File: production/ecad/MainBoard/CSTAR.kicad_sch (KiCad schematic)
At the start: 0 parts

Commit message: Button + RGB IO schematic
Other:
- added sheet CSTAR-IO (cstar-io.kicad_sch)
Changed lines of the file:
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@@
+    )
+  )
+  (sheet (at 191.77 99.06) (size 18.415 15.24) (fields_autoplaced)
+    (stroke (width 0.1524) (type solid))
+    (fill (color 0 0 0 0.0000))
+    (property "Sheetname" "CSTAR-IO" (at 191.77 98.3484 0)
+      (effects (font (size 1.27 1.27)) (justify left bottom))
+    )
+    (property "Sheetfile" "cstar-io.kicad_sch" (at 191.77 114.8846 0)
+      (effects (font (size 1.27 1.27)) (justify left top))
+    )
+    (instances
+      (project "CSTAR"
+        (path "/cd9fa943-c6eb-468b-990c-ea873c442553" (page "7"))
+      )
     )
   )

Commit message: Update of gitignore and main sch
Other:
- sheet CSTAR-Drive ports: added Ch.A Motor 1, Ch.A Motor 2, Ch.B Motor 1, Ch.B Motor 2, DECAY MOTOR 1, DECAY MOTOR 2, GND Motor 1, GND Motor 2, I0 MOTOR 1, I0 MOTOR 2, I1 MOTOR 1, I1 MOTOR 2, I2 MOTOR 1, I2 MOTOR 2, I3 MOTOR 1, I3 MOTOR 2, I4 MOTOR 1, I4 MOTOR 2, IN1 MOTOR 1, IN1 MOTOR 2, IN2 MOTOR 1, IN2 MOTOR 2, OUT1 MOTOR 1, OUT1 MOTOR 2, OUT2 MOTOR 1, OUT2 MOTOR 2, VCC Motor 1, VCC Motor 2, nFAULT MOTOR 1, nFAULT MOTOR 2, nRESET MOTOR 1, nRESET MOTOR 2, nSLEEP MOTOR 1, nSLEEP MOTOR 2; removed none
- sheet CSTAR-IO ports: added BATT_IN, RBG_Green_Control, RGB_Blue_Control, RGB_Red_Control; removed none
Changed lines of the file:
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@@
     )
   )
-  (sheet (at 191.77 99.06) (size 18.415 15.24) (fields_autoplaced)
+  (sheet (at 191.77 99.06) (size 34.925 27.305) (fields_autoplaced)
     (stroke (width 0.1524) (type solid))
     (fill (color 0 0 0 0.0000))
@@
       (effects (font (size 1.27 1.27)) (justify left bottom))
     )
-    (property "Sheetfile" "cstar-io.kicad_sch" (at 191.77 114.8846 0)
+    (property "Sheetfile" "cstar-io.kicad_sch" (at 191.77 126.9496 0)
       (effects (font (size 1.27 1.27)) (justify left top))
+    )
+    (pin "RGB_Red_Control" input (at 191.77 104.14 180)
+      (effects (font (size 1.27 1.27)) (justify left))
+    )
+    (pin "RBG_Green_Control" input (at 191.77 110.49 180)
+      (effects (font (size 1.27 1.27)) (justify left))
+    )
+    (pin "RGB_Blue_Control" input (at 191.77 116.84 180)
+      (effects (font (size 1.27 1.27)) (justify left))
+    )
+    (pin "BATT_IN" input (at 226.695 104.14 0)
+      (effects (font (size 1.27 1.27)) (justify right))
     )
     (instances
@@
     )
   )
-  (sheet (at 179.705 29.845) (size 45.085 45.085) (fields_autoplaced)
+  (sheet (at 172.72 20.32) (size 71.12 61.595) (fields_autoplaced)
     (stroke (width 0.1524) (type solid))
     (fill (color 0 0 0 0.0000))
-    (property "Sheetname" "CSTAR-Drive" (at 179.705 29.1334 0)
+    (property "Sheetname" "CSTAR-Drive" (at 172.72 19.6084 0)
       (effects (font (size 1.27 1.27)) (justify left bottom))
     )
-    (property "Sheetfile" "cstar-drive.kicad_sch" (at 179.705 75.5146 0)
+    (property "Sheetfile" "cstar-drive.kicad_sch" (at 172.72 82.4996 0)
       (effects (font (size 1.27 1.27)) (justify left top))
     )
+    (pin "Ch.B Motor 1" input (at 172.72 22.86 180)
+      (effects (font (size 1.27 1.27)) (justify left))
+    )
+    (pin "OUT1 MOTOR 1" passive (at 243.84 37.465 0)
+      (effects (font (size 1.27 1.27)) (justify right))
+    )
+    (pin "OUT2 MOTOR 1" passive (at 243.84 43.815 0)
+      (effects (font (size 1.27 1.27)) (justify right))
+    )
+    (pin "VCC Motor 1" input (at 243.84 24.765 0)
+      (effects (font (size 1.27 1.27)) (justify right))
+    )
+    (pin "Ch.A Motor 1" input (at 172.72 26.035 180)
+      (effects (font (size 1.27 1.27)) (justify left))
+    )
+    (pin "GND Motor 1" input (at 243.84 76.2 0)
+      (effects (font (size 1.27 1.27)) (justify right))
+    )
+    (pin "OUT2 MOTOR 2" passive (at 243.84 50.8 0)
+      (effects (font (size 1.27 1.27)) (justify right))
+    )
+    (pin "OUT1 MOTOR 2" passive (at 243.84 56.515 0)
+      (effects (font (size 1.27 1.27)) (justify right))
+    )
+    (pin "IN1 MOTOR 2" input (at 172.72 31.75 180)
+      (effects (font (size 1.27 1.27)) (justify left))
+    )
+    (pin "nFAULT MOTOR 1" output (at 172.72 34.29 180)
+      (effects (font (size 1.27 1.27)) (justify left))
+    )
+    (pin "nFAULT MOTOR 2" output (at 172.72 44.45 180)
+      (effects (font (size 1.27 1.27)) (justify left))
+    )
+    (pin "DECAY MOTOR 2" input (at 172.72 52.07 180)
+      (effects (font (size 1.27 1.27)) (justify left))
+    )
+    (pin "I0 MOTOR 2" input (at 172.72 46.99 180)
+      (effects (font (size 1.27 1.27)) (justify left))
+    )
+    (pin "nSLEEP MOTOR 2" input (at 172.72 49.53 180)
+      (effects (font (size 1.27 1.27)) (justify left))
+    )
+    (pin "I2 MOTOR 2" input (at 172.72 41.91 180)
+      (effects (font (size 1.27 1.27)) (justify left))
+    )
+    (pin "nRESET MOTOR 2" input (at 172.72 54.61 180)
+      (effects (font (size 1.27 1.27)) (justify left))
+    )
+    (pin "I3 MOTOR 2" input (at 172.72 39.37 180)
+      (effects (font (size 1.27 1.27)) (justify left))
+    )
+    (pin "I4 MOTOR 2" input (at 172.72 60.325 180)
+      (effects (font (size 1.27 1.27)) (justify left))
+    )
+    (pin "I1 MOTOR 2" input (at 172.72 68.58 180)
+      (effects (font (size 1.27 1.27)) (justify left))
+    )
+    (pin "IN2 MOTOR 2" input (at 172.72 71.12 180)
+      (effects (font (size 1.27 1.27)) (justify left))
+    )
+    (pin "GND Motor 2" input (at 172.72 73.66 180)
+      (effects (font (size 1.27 1.27)) (justify left))
+    )
+    (pin "Ch.B Motor 2" input (at 172.72 76.2 180)
+      (effects (font (size 1.27 1.27)) (justify left))
+    )
+    (pin "Ch.A Motor 2" input (at 172.72 78.74 180)
+      (effects (font (size 1.27 1.27)) (justify left))
+    )
+    (pin "VCC Motor 2" input (at 243.84 27.94 0)
+      (effects (font (size 1.27 1.27)) (justify right))
+    )
+    (pin "DECAY MOTOR 1" input (at 198.12 81.915 270)
+      (effects (font (size 1.27 1.27)) (justify left))
+    )
+    (pin "I4 MOTOR 1" input (at 201.93 81.915 270)
+      (effects (font (size 1.27 1.27)) (justify left))
+    )
+    (pin "nRESET MOTOR 1" input (at 201.93 81.915 270)
+      (effects (font (size 1.27 1.27)) (justify left))
+    )
+    (pin "nSLEEP MOTOR 1" input (at 206.375 81.915 270)
+      (effects (font (size 1.27 1.27)) (justify left))
+    )
+    (pin "IN2 MOTOR 1" input (at 210.185 81.915 270)
+      (effects (font (size 1.27 1.27)) (justify left))
+    )
+    (pin "I0 MOTOR 1" input (at 214.63 81.915 270)
+      (effects (font (size 1.27 1.27)) (justify left))
+    )
+    (pin "IN1 MOTOR 1" input (at 215.265 81.915 270)
+      (effects (font (size 1.27 1.27)) (justify left))
+    )
+    (pin "I3 MOTOR 1" input (at 219.075 81.915 270)
+      (effects (font (size 1.27 1.27)) (justify left))
+    )
+    (pin "I2 MOTOR 1" input (at 223.52 81.915 270)
+      (effects (font (size 1.27 1.27)) (justify left))
+    )
+    (pin "I1 MOTOR 1" input (at 227.965 81.915 270)
+      (effects (font (size 1.27 1.27)) (justify left))
+    )
     (instances

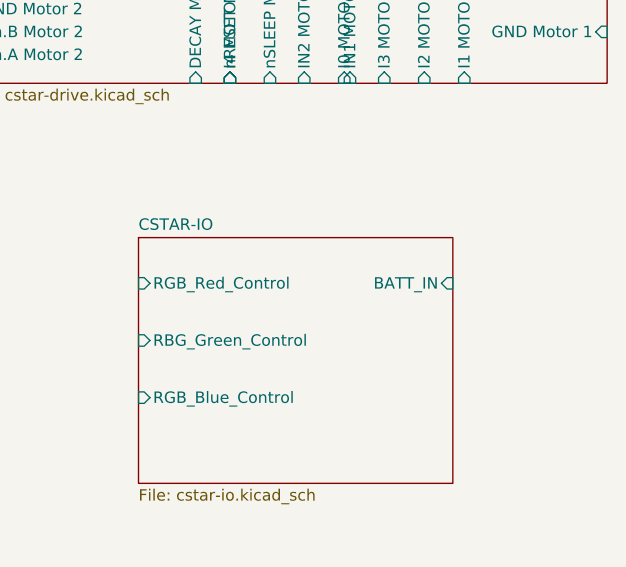
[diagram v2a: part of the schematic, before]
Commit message: updated battery connection net name
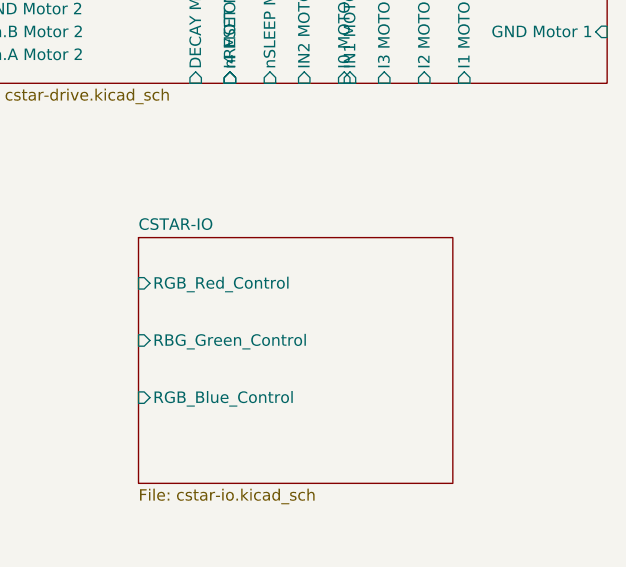
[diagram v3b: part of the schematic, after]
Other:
- sheet CSTAR-IO ports: added none; removed BATT_IN
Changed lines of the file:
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@@
       (effects (font (size 1.27 1.27)) (justify left))
-    )
-    (pin "BATT_IN" input (at 226.695 104.14 0)
-      (effects (font (size 1.27 1.27)) (justify right))
     )
     (instances

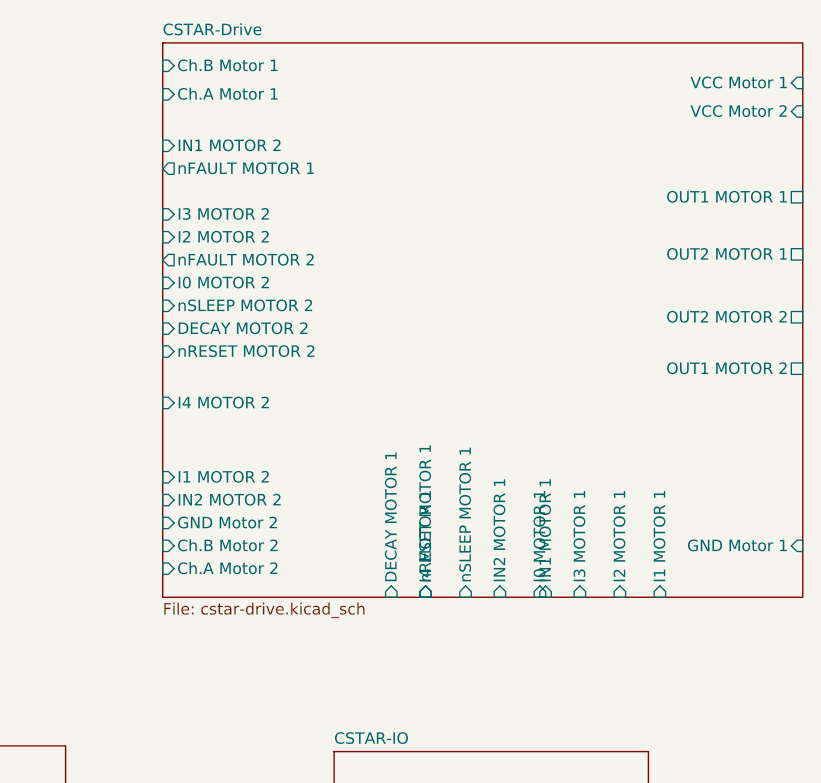
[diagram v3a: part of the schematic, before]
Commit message: updated hierarchical schematics
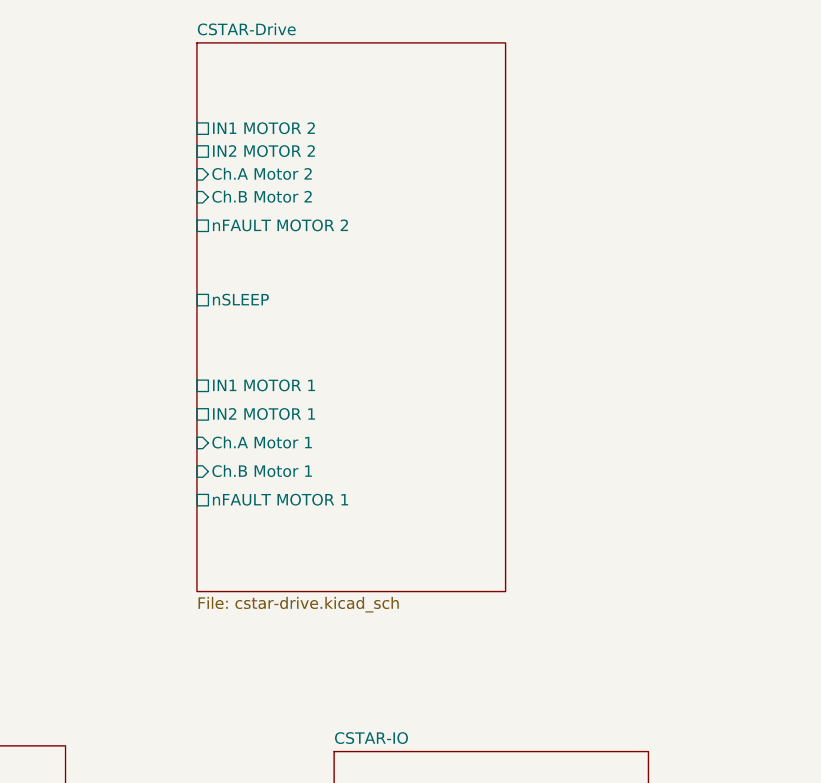
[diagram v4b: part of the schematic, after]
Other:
- sheet CSTAR-Drive ports: added nSLEEP; removed DECAY MOTOR 1, DECAY MOTOR 2, GND Motor 1, GND Motor 2, I0 MOTOR 1, I0 MOTOR 2, I1 MOTOR 1, I1 MOTOR 2, I2 MOTOR 1, I2 MOTOR 2, I3 MOTOR 1, I3 MOTOR 2, I4 MOTOR 1, I4 MOTOR 2, OUT1 MOTOR 1, OUT1 MOTOR 2, OUT2 MOTOR 1, OUT2 MOTOR 2, VCC Motor 1, VCC Motor 2, nRESET MOTOR 1, nRESET MOTOR 2, nSLEEP MOTOR 1, nSLEEP MOTOR 2
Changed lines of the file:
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@@
     )
   )
-  (sheet (at 172.72 20.32) (size 71.12 61.595) (fields_autoplaced)
+  (sheet (at 176.53 20.32) (size 34.29 60.96) (fields_autoplaced)
     (stroke (width 0.1524) (type solid))
     (fill (color 0 0 0 0.0000))
-    (property "Sheetname" "CSTAR-Drive" (at 172.72 19.6084 0)
+    (property "Sheetname" "CSTAR-Drive" (at 176.53 19.6084 0)
       (effects (font (size 1.27 1.27)) (justify left bottom))
     )
-    (property "Sheetfile" "cstar-drive.kicad_sch" (at 172.72 82.4996 0)
+    (property "Sheetfile" "cstar-drive.kicad_sch" (at 176.53 81.8646 0)
       (effects (font (size 1.27 1.27)) (justify left top))
     )
-    (pin "Ch.B Motor 1" input (at 172.72 22.86 180)
+    (pin "IN1 MOTOR 2" passive (at 176.53 29.845 180)
       (effects (font (size 1.27 1.27)) (justify left))
     )
-    (pin "OUT1 MOTOR 1" passive (at 243.84 37.465 0)
-      (effects (font (size 1.27 1.27)) (justify right))
-    )
-    (pin "OUT2 MOTOR 1" passive (at 243.84 43.815 0)
-      (effects (font (size 1.27 1.27)) (justify right))
-    )
-    (pin "VCC Motor 1" input (at 243.84 24.765 0)
-      (effects (font (size 1.27 1.27)) (justify right))
-    )
-    (pin "Ch.A Motor 1" input (at 172.72 26.035 180)
+    (pin "IN2 MOTOR 2" passive (at 176.53 32.385 180)
       (effects (font (size 1.27 1.27)) (justify left))
     )
-    (pin "GND Motor 1" input (at 243.84 76.2 0)
-      (effects (font (size 1.27 1.27)) (justify right))
-    )
-    (pin "OUT2 MOTOR 2" passive (at 243.84 50.8 0)
-      (effects (font (size 1.27 1.27)) (justify right))
-    )
-    (pin "OUT1 MOTOR 2" passive (at 243.84 56.515 0)
-      (effects (font (size 1.27 1.27)) (justify right))
-    )
-    (pin "IN1 MOTOR 2" input (at 172.72 31.75 180)
+    (pin "nSLEEP" passive (at 176.53 48.895 180)
       (effects (font (size 1.27 1.27)) (justify left))
     )
-    (pin "nFAULT MOTOR 1" output (at 172.72 34.29 180)
+    (pin "nFAULT MOTOR 2" passive (at 176.53 40.64 180)
       (effects (font (size 1.27 1.27)) (justify left))
     )
-    (pin "nFAULT MOTOR 2" output (at 172.72 44.45 180)
+    (pin "nFAULT MOTOR 1" passive (at 176.53 71.12 180)
       (effects (font (size 1.27 1.27)) (justify left))
     )
-    (pin "DECAY MOTOR 2" input (at 172.72 52.07 180)
+    (pin "Ch.A Motor 1" input (at 176.53 64.77 180)
       (effects (font (size 1.27 1.27)) (justify left))
     )
-    (pin "I0 MOTOR 2" input (at 172.72 46.99 180)
+    (pin "Ch.B Motor 1" input (at 176.53 67.945 180)
       (effects (font (size 1.27 1.27)) (justify left))
     )
-    (pin "nSLEEP MOTOR 2" input (at 172.72 49.53 180)
+    (pin "Ch.B Motor 2" input (at 176.53 37.465 180)
       (effects (font (size 1.27 1.27)) (justify left))
     )
-    (pin "I2 MOTOR 2" input (at 172.72 41.91 180)
+    (pin "Ch.A Motor 2" input (at 176.53 34.925 180)
       (effects (font (size 1.27 1.27)) (justify left))
     )
-    (pin "nRESET MOTOR 2" input (at 172.72 54.61 180)
+    (pin "IN2 MOTOR 1" passive (at 176.53 61.595 180)
       (effects (font (size 1.27 1.27)) (justify left))
     )
-    (pin "I3 MOTOR 2" input (at 172.72 39.37 180)
+    (pin "IN1 MOTOR 1" passive (at 176.53 58.42 180)
       (effects (font (size 1.27 1.27)) (justify left))
     )
-    (pin "I4 MOTOR 2" input (at 172.72 60.325 180)
-      (effects (font (size 1.27 1.27)) (justify left))
-    )
-    (pin "I1 MOTOR 2" input (at 172.72 68.58 180)
-      (effects (font (size 1.27 1.27)) (justify left))
-    )
-    (pin "IN2 MOTOR 2" input (at 172.72 71.12 180)
-      (effects (font (size 1.27 1.27)) (justify left))
-    )
-    (pin "GND Motor 2" input (at 172.72 73.66 180)
-      (effects (font (size 1.27 1.27)) (justify left))
-    )
-    (pin "Ch.B Motor 2" input (at 172.72 76.2 180)
-      (effects (font (size 1.27 1.27)) (justify left))
-    )
-    (pin "Ch.A Motor 2" input (at 172.72 78.74 180)
-      (effects (font (size 1.27 1.27)) (justify left))
-    )
-    (pin "VCC Motor 2" input (at 243.84 27.94 0)
-      (effects (font (size 1.27 1.27)) (justify right))
-    )
-    (pin "DECAY MOTOR 1" input (at 198.12 81.915 270)
-      (effects (font (size 1.27 1.27)) (justify left))
-    )
-    (pin "I4 MOTOR 1" input (at 201.93 81.915 270)
-      (effects (font (size 1.27 1.27)) (justify left))
-    )
-    (pin "nRESET MOTOR 1" input (at 201.93 81.915 270)
-      (effects (font (size 1.27 1.27)) (justify left))
-    )
-    (pin "nSLEEP MOTOR 1" input (at 206.375 81.915 270)
-      (effects (font (size 1.27 1.27)) (justify left))
-    )
-    (pin "IN2 MOTOR 1" input (at 210.185 81.915 270)
-      (effects (font (size 1.27 1.27)) (justify left))
-    )
-    (pin "I0 MOTOR 1" input (at 214.63 81.915 270)
-      (effects (font (size 1.27 1.27)) (justify left))
-    )
-    (pin "IN1 MOTOR 1" input (at 215.265 81.915 270)
-      (effects (font (size 1.27 1.27)) (justify left))
-    )
-    (pin "I3 MOTOR 1" input (at 219.075 81.915 270)
-      (effects (font (size 1.27 1.27)) (justify left))
-    )
-    (pin "I2 MOTOR 1" input (at 223.52 81.915 270)
-      (effects (font (size 1.27 1.27)) (justify left))
-    )
-    (pin "I1 MOTOR 1" input (at 227.965 81.915 270)
-      (effects (font (size 1.27 1.27)) (justify left))
-    )

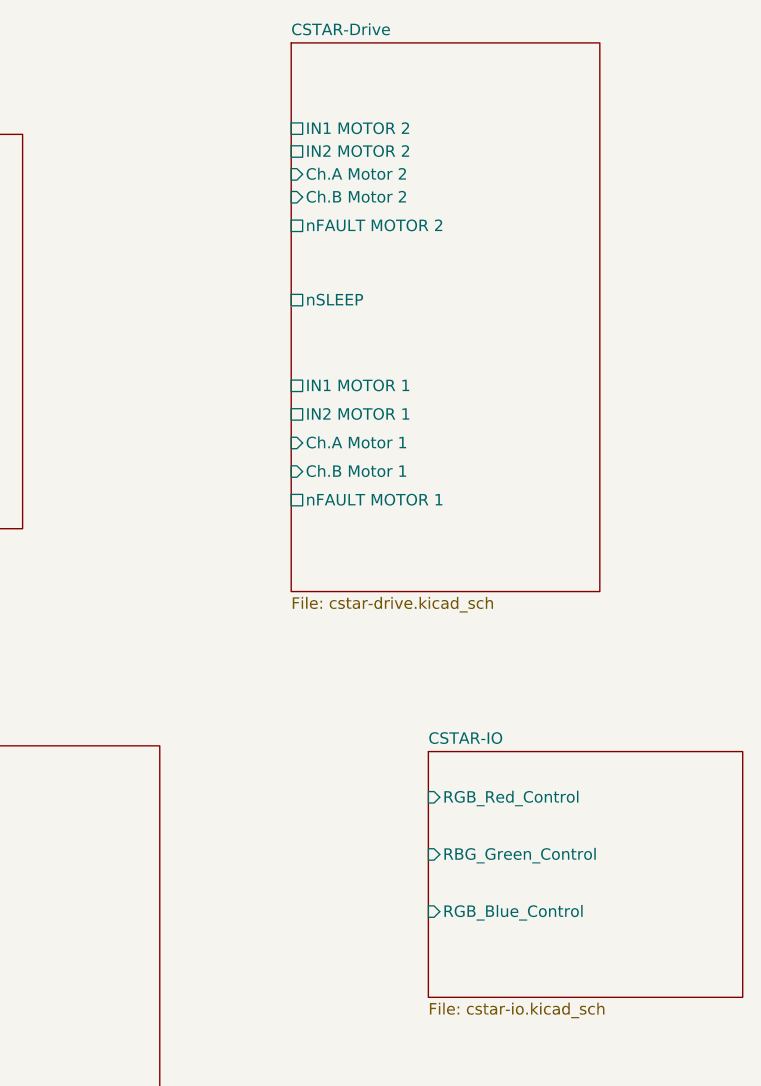
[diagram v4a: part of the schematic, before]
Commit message: annoted schematic and change diode back to res
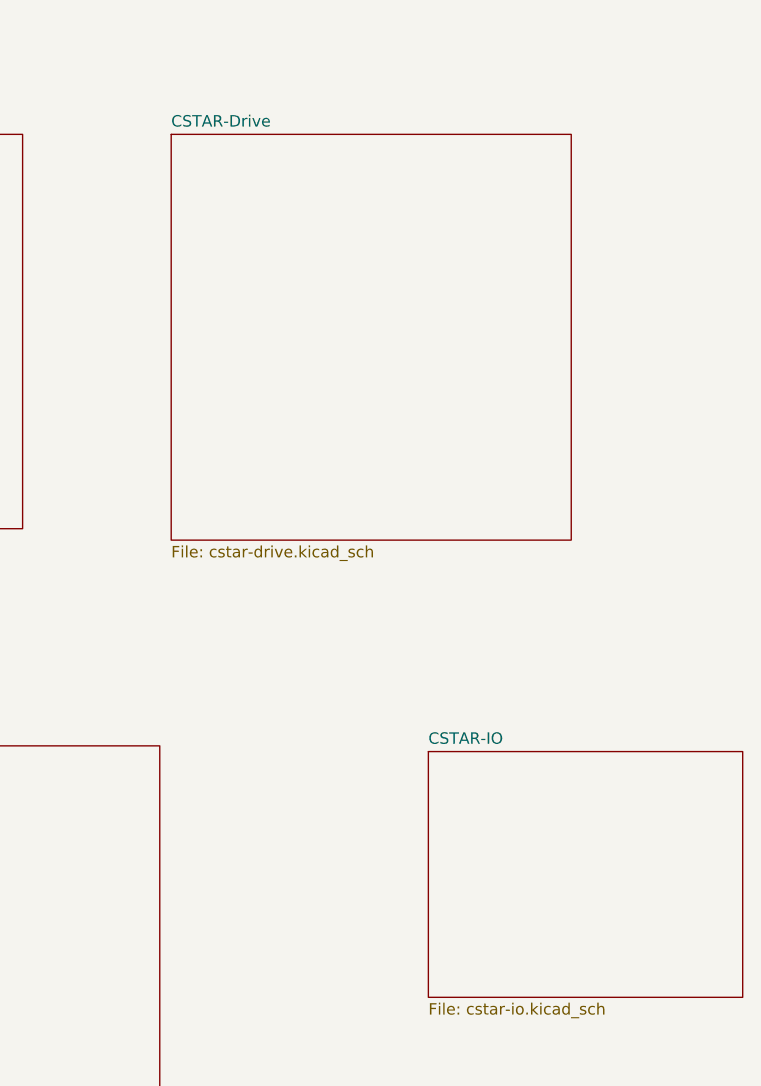
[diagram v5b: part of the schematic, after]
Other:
- sheet CSTAR-Drive ports: added none; removed Ch.A Motor 1, Ch.A Motor 2, Ch.B Motor 1, Ch.B Motor 2, IN1 MOTOR 1, IN1 MOTOR 2, IN2 MOTOR 1, IN2 MOTOR 2, nFAULT MOTOR 1, nFAULT MOTOR 2, nSLEEP
- sheet CSTAR-IO ports: added none; removed RBG_Green_Control, RGB_Blue_Control, RGB_Red_Control
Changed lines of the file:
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@@
       (effects (font (size 1.27 1.27)) (justify left top))
-    )
-    (pin "RGB_Red_Control" input (at 191.77 104.14 180)
-      (effects (font (size 1.27 1.27)) (justify left))
-    )
-    (pin "RBG_Green_Control" input (at 191.77 110.49 180)
-      (effects (font (size 1.27 1.27)) (justify left))
-    )
-    (pin "RGB_Blue_Control" input (at 191.77 116.84 180)
-      (effects (font (size 1.27 1.27)) (justify left))
     )
     (instances
@@
     )
   )
-  (sheet (at 176.53 20.32) (size 34.29 60.96) (fields_autoplaced)
+  (sheet (at 163.195 30.48) (size 44.45 45.085) (fields_autoplaced)
     (stroke (width 0.1524) (type solid))
     (fill (color 0 0 0 0.0000))
-    (property "Sheetname" "CSTAR-Drive" (at 176.53 19.6084 0)
+    (property "Sheetname" "CSTAR-Drive" (at 163.195 29.7684 0)
       (effects (font (size 1.27 1.27)) (justify left bottom))
     )
-    (property "Sheetfile" "cstar-drive.kicad_sch" (at 176.53 81.8646 0)
+    (property "Sheetfile" "cstar-drive.kicad_sch" (at 163.195 76.1496 0)
       (effects (font (size 1.27 1.27)) (justify left top))
     )
-    (pin "IN1 MOTOR 2" passive (at 176.53 29.845 180)
-      (effects (font (size 1.27 1.27)) (justify left))
-    )
-    (pin "IN2 MOTOR 2" passive (at 176.53 32.385 180)
-      (effects (font (size 1.27 1.27)) (justify left))
-    )
-    (pin "nSLEEP" passive (at 176.53 48.895 180)
-      (effects (font (size 1.27 1.27)) (justify left))
-    )
-    (pin "nFAULT MOTOR 2" passive (at 176.53 40.64 180)
-      (effects (font (size 1.27 1.27)) (justify left))
-    )
-    (pin "nFAULT MOTOR 1" passive (at 176.53 71.12 180)
-      (effects (font (size 1.27 1.27)) (justify left))
-    )
-    (pin "Ch.A Motor 1" input (at 176.53 64.77 180)
-      (effects (font (size 1.27 1.27)) (justify left))
-    )
-    (pin "Ch.B Motor 1" input (at 176.53 67.945 180)
-      (effects (font (size 1.27 1.27)) (justify left))
-    )
-    (pin "Ch.B Motor 2" input (at 176.53 37.465 180)
-      (effects (font (size 1.27 1.27)) (justify left))
-    )
-    (pin "Ch.A Motor 2" input (at 176.53 34.925 180)
-      (effects (font (size 1.27 1.27)) (justify left))
-    )
-    (pin "IN2 MOTOR 1" passive (at 176.53 61.595 180)
-      (effects (font (size 1.27 1.27)) (justify left))
-    )
-    (pin "IN1 MOTOR 1" passive (at 176.53 58.42 180)
-      (effects (font (size 1.27 1.27)) (justify left))
-    )
     (instances
